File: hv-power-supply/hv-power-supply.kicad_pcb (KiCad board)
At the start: 2 copper layers, 44.5 x 34.3 mm, 27 parts, among them J1 Conn_01x01, J2 Conn_01x01, J3 Conn_01x01, J4 Conn_01x01, Q1 PSMN014-80YL, T1 NA5920-AL, U1 TPS40210

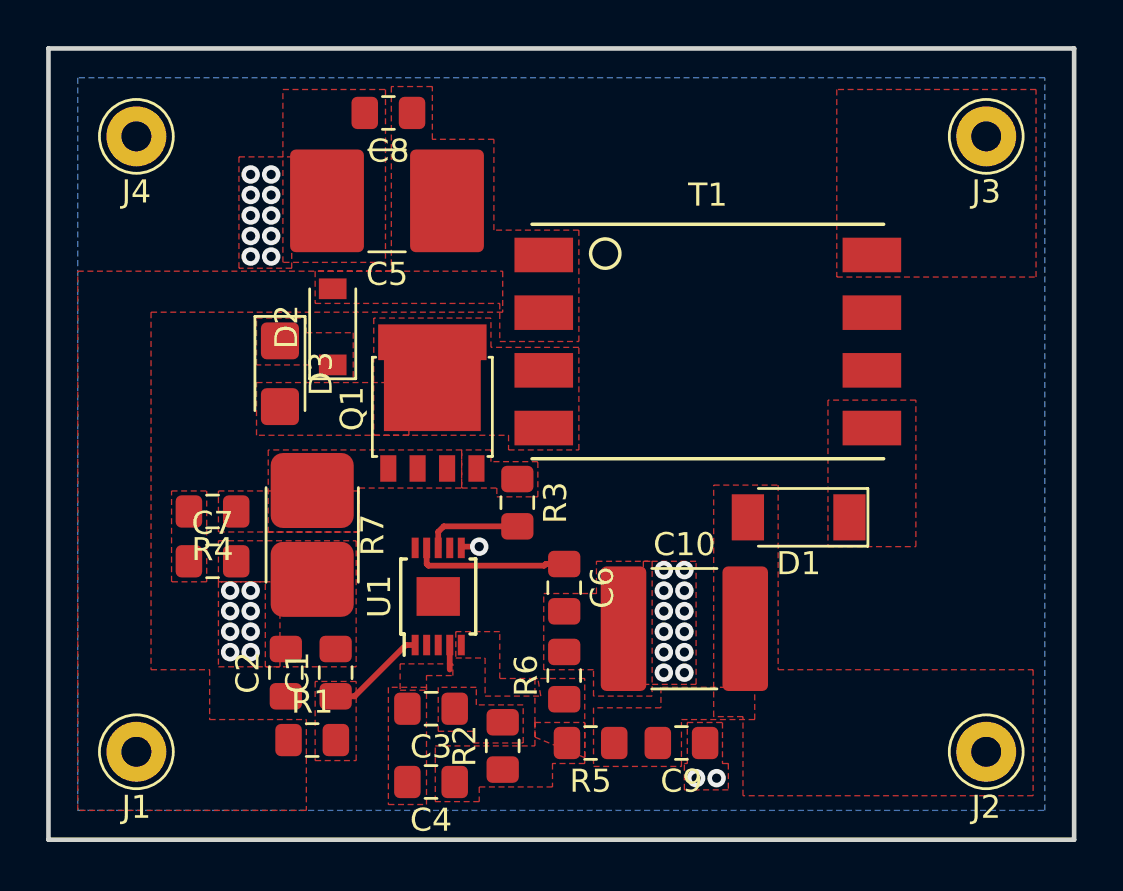
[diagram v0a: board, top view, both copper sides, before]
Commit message: Initial spin of hv power supply test board
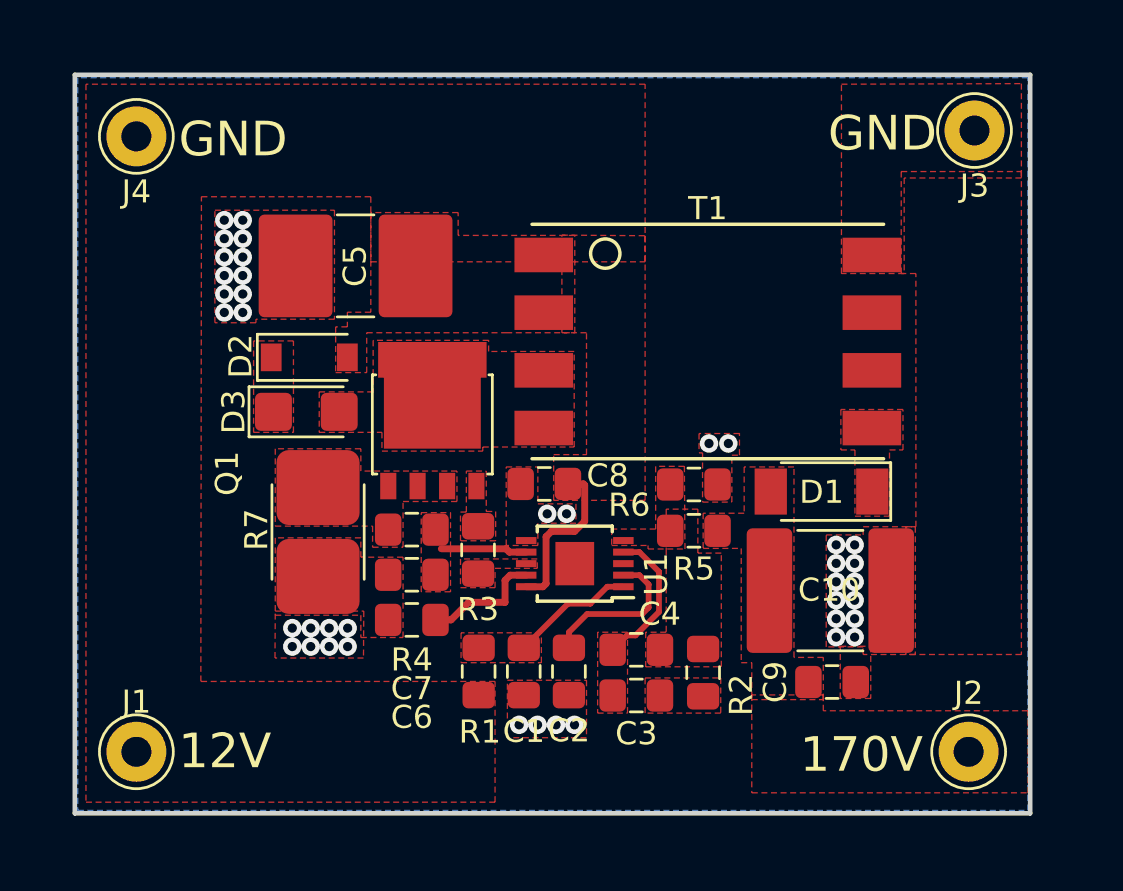
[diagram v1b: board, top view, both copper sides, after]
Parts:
- moved C8 17.4 mm to (85.0, 74.8)
- moved C2 12.3 mm to (86.1, 82.9), turned to 270 degrees
- moved C4 10.6 mm to (89.0, 81.9)
- moved R5 10.2 mm to (91.5, 76.8)
- moved R6 10.0 mm to (91.5, 74.8), turned to 0 degrees
- moved R2 9.25 mm to (91.9, 82.9), turned to 270 degrees
- moved C3 8.92 mm to (89.0, 83.9)
- moved R4 8.67 mm to (79.2, 76.7), turned to 0 degrees
- moved C7 8.66 mm to (79.2, 78.7), turned to 180 degrees
- moved C1 8.15 mm to (84.1, 82.9), turned to 270 degrees
- moved R1 7.80 mm to (82.1, 82.9), turned to 90 degrees
- moved C9 7.04 mm to (97.5, 83.3)
- moved C6 6.75 mm to (79.2, 80.6), turned to 180 degrees
- moved C10 6.54 mm to (97.4, 79.4), turned to 180 degrees
- moved U1 6.09 mm to (86.3, 78.2), turned to 180 degrees
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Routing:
- net VDD: track 0.00 -> 7.22 mm
- net Net-(C2-Pad1): track 0.00 -> 6.84 mm
- net Net-(C3-Pad2): track 1.06 -> 6.33 mm
- net Net-(R3-Pad2): track 4.22 -> 0.00 mm
- net Net-(C7-Pad1): track 0.00 -> 3.74 mm
- net Net-(C6-Pad1): track 6.72 -> 5.29 mm
- net Net-(C1-Pad1): track 4.37 -> 5.41 mm
- net GND: track 0.80 -> 0.00 mm, vias 33 -> 40
- added copper zone on F.Cu, net Net-(R3-Pad2)
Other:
- board size 44.5 x 34.3 mm -> 41.4 x 32 mm
- net class Default: clearance 0.2 -> 0.1524; trace_width 0.25 -> 0.1524; via_dia 0.8 -> 0.6858; via_drill 0.4 -> 0.3302
- rule trace_clearance: 0.2 -> 0.1524
- rule trace_min: 0.2 -> 0.1524
- rule via_min_drill: 0.3 -> 0.254
- rule via_min_size: 0.4 -> 0.508
- board text added: "12V"
- board text added: "170V"
- board text added: "GND"

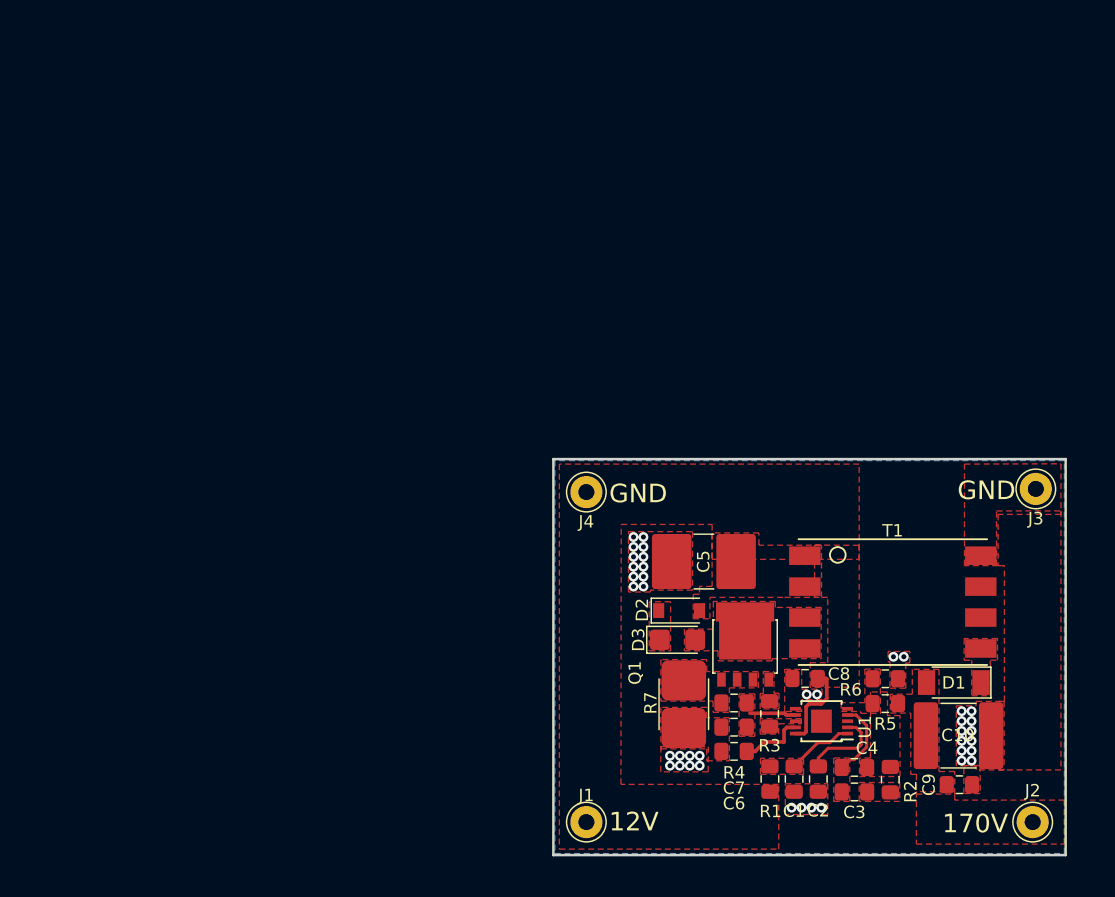
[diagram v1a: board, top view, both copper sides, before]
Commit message: Fix lots of layout issues in high voltage power supply
1. Don't route power through bottom layer ground plane
2. Make sure U1 grounding pad is connected
3. Kelvin connections for current sense resistor
4. Pour keepouts under transformer
5. Keep voltage feedback divider near IC
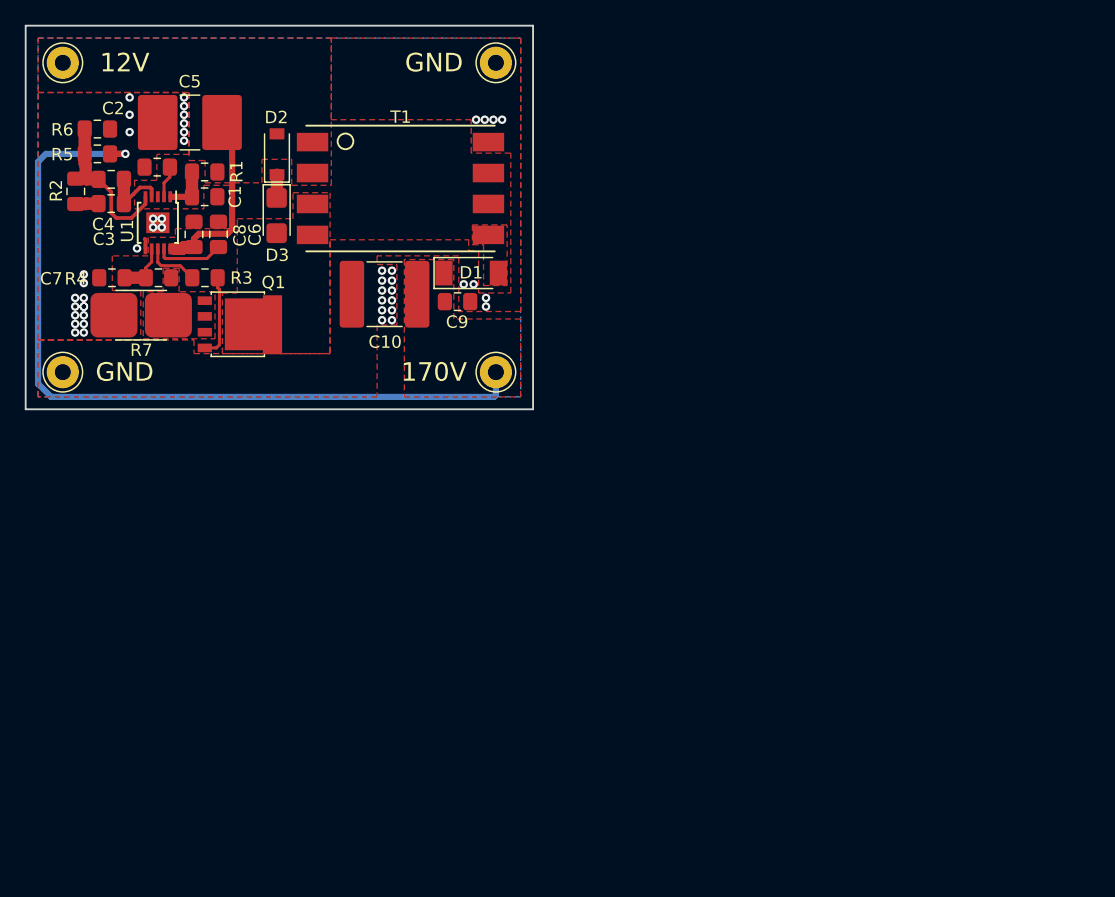
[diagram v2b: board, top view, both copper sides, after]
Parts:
- moved R2 81.2 mm to (26.1, 35.4)
- moved R5 77.6 mm to (27.8, 32.4)
- moved R6 77.6 mm to (27.8, 30.4)
- moved C3 76.6 mm to (28.9, 36.4), turned to 0 degrees
- moved C4 76.6 mm to (28.9, 34.4), turned to 0 degrees
- moved J1 74.5 mm to (25.0, 25.0)
- moved C2 72.8 mm to (32.6, 33.4), turned to 180 degrees
- moved U1 67.1 mm to (32.7, 37.9), turned to 270 degrees
- moved R1 67.0 mm to (36.5, 33.8), turned to 180 degrees
- moved C1 67.0 mm to (36.5, 35.8), turned to 0 degrees
- moved C7 62.0 mm to (29.0, 42.4)
- moved C8 61.0 mm to (35.6, 38.9), turned to 90 degrees
- moved C6 59.0 mm to (37.6, 38.9), turned to 90 degrees
- moved C10 58.5 mm to (51.0, 43.7), turned to 0 degrees
- moved R4 57.8 mm to (32.7, 42.4), turned to 180 degrees
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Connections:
- D1 pad 1: Net-(D1-Pad1) -> +170V
- D1 pad 2: +170V -> Net-(D1-Pad2)
- T1 pad 5: Net-(D1-Pad1) -> Net-(D1-Pad2)
- U1 pad 11: (no net) -> GND
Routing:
- net +170V: track 0.00 -> 65.8 mm, vias 0 -> 1
- net Net-(C4-Pad1): track 0.00 -> 13.0 mm
- net Net-(Q1-Pad4): track 0.00 -> 6.77 mm
- net VDD: track 7.22 -> 13.5 mm
- net Net-(R3-Pad2): track 0.00 -> 4.39 mm
- net Net-(C2-Pad1): track 6.84 -> 2.57 mm
- net Net-(D2-Pad1): track 0.00 -> 2.11 mm
- net Net-(C3-Pad1): track 0.00 -> 1.85 mm
- net Net-(C1-Pad1): track 5.41 -> 3.69 mm
- net Net-(C3-Pad2): track 6.33 -> 5.41 mm
- net GND: track 0.00 -> 0.83 mm, vias 40 -> 48
- net Net-(C7-Pad1): track 3.74 -> 4.25 mm
- added copper zone on F.Cu, net Net-(D1-Pad2)
- removed copper zone on F.Cu, net Net-(C1-Pad1)
- removed copper zone on F.Cu, net Net-(C3-Pad1)
- removed copper zone on F.Cu, net Net-(C3-Pad2)
- removed copper zone on F.Cu, net Net-(C4-Pad1)
- removed copper zone on F.Cu, net Net-(C7-Pad1)
- removed copper zone on F.Cu, net Net-(D1-Pad1)
- removed copper zone on F.Cu, net Net-(D2-Pad1)
- removed copper zone on F.Cu, net Net-(Q1-Pad4)
- removed copper zone on F.Cu, net Net-(R3-Pad2)
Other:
- board size 41.4 x 32 mm -> 41 x 31 mm
